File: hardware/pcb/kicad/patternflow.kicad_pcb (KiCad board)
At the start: 2 copper layers, 74 x 132.5 mm, 9 parts, among them J1 Conn_02x08_Odd_Even, J2 Screw_Terminal_01x02, J3 Screw_Terminal_01x02, SW1 RotaryEncoder_Switch, SW2 RotaryEncoder_Switch, SW3 RotaryEncoder_Switch, SW4 RotaryEncoder_Switch, U1 ESP32-S3-DevKit-44pin

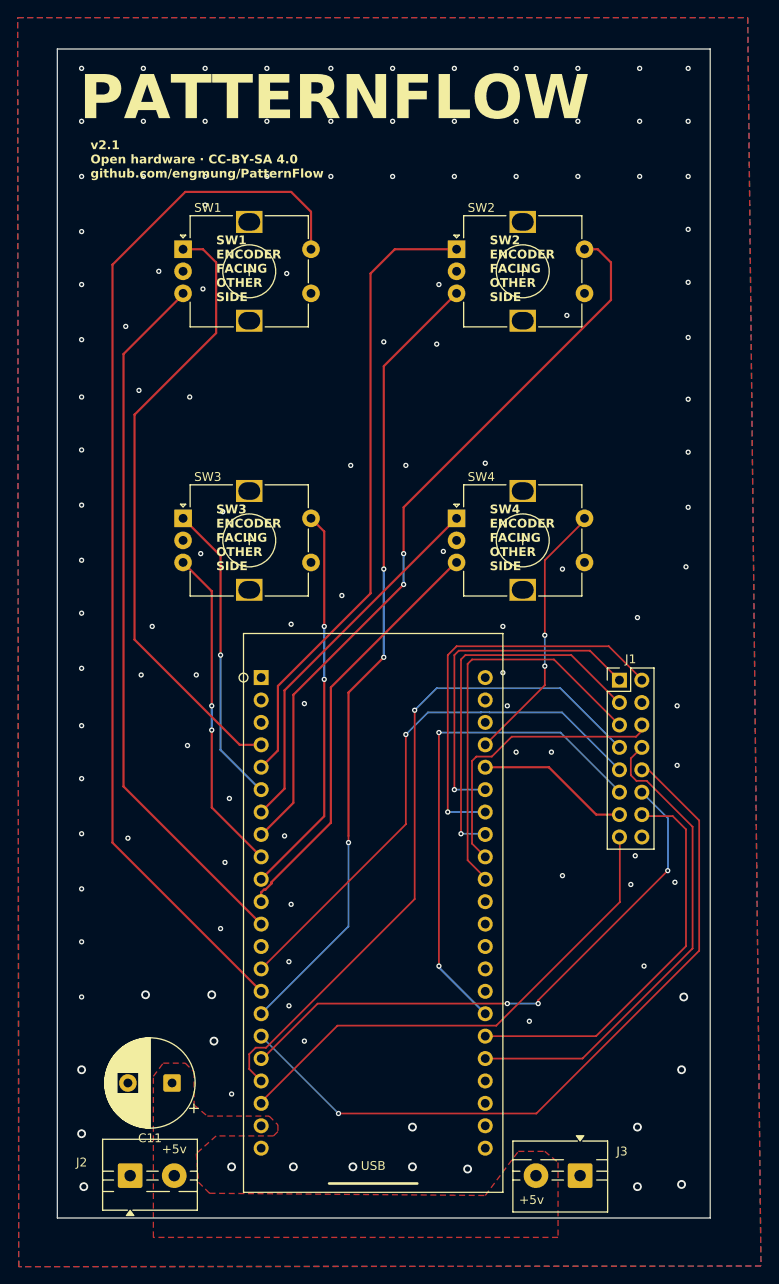
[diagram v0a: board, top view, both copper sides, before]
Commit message: refactor(repo): update github repository casing from PatternFlow to Patternflow
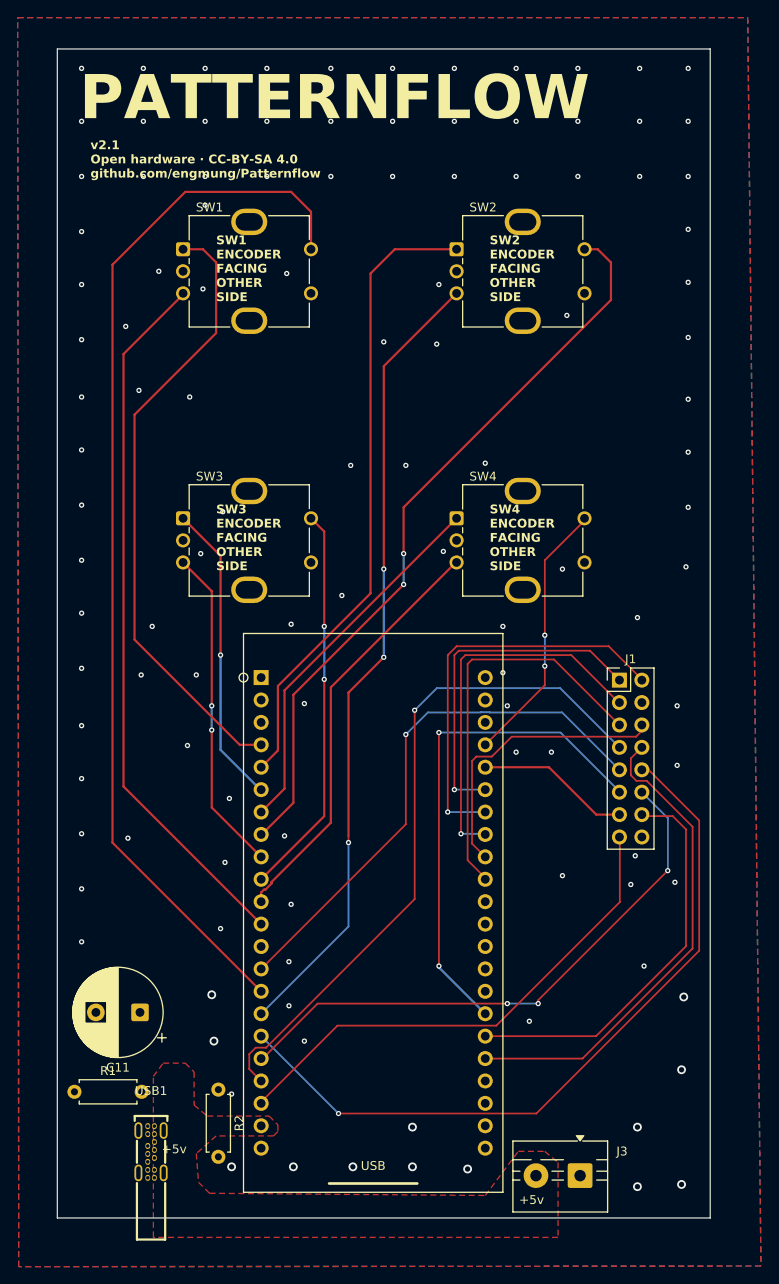
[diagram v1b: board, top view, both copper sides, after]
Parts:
- removed J2: Screw_Terminal_01x02, TerminalBlock:TerminalBlock_MaiXu_MX126-5.0-02P_1x02_P5.00mm
- added R1: 5.1k, Resistor_THT:R_Axial_DIN0207_L6.3mm_D2.5mm_P7.62mm_Horizontal, F.Cu at (55.9, 147.0)
- added R2: 5.1k, Resistor_THT:R_Axial_DIN0207_L6.3mm_D2.5mm_P7.62mm_Horizontal, F.Cu at (72.2, 146.8)
- added USB1: TYPE-C 14P CC-2.6, patternflow:TYPE-C-TH_TYPE-C-14P-CC-2.6, F.Cu at (64.6, 153.8)
- SW1, SW2, SW3, SW4: footprint Rotary_Encoder:RotaryEncoder_Alps_EC12E-Switch_Vertical_H20mm -> Rotary_Encoder:RotaryEncoder_Bourns_Vertical_PEC12R-3x17F-Sxxxx
- moved C11 8.79 mm to (63.4, 138.0)
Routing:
- net GND: vias 121 -> 116
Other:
- board text added: "v2.1 Open hardware · CC-BY-SA 4.0 github.com/engmung/Patternflow"
- board text removed: "v2.1 Open hardware · CC-BY-SA 4.0 github.com/engmung/PatternFlow"
